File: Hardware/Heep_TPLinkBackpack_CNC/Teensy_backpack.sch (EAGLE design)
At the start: 32 parts, among them J1 FEMALE 2x3, Q1 25MHz, Q2 600mA/40V, U1 ENC28J60-SO

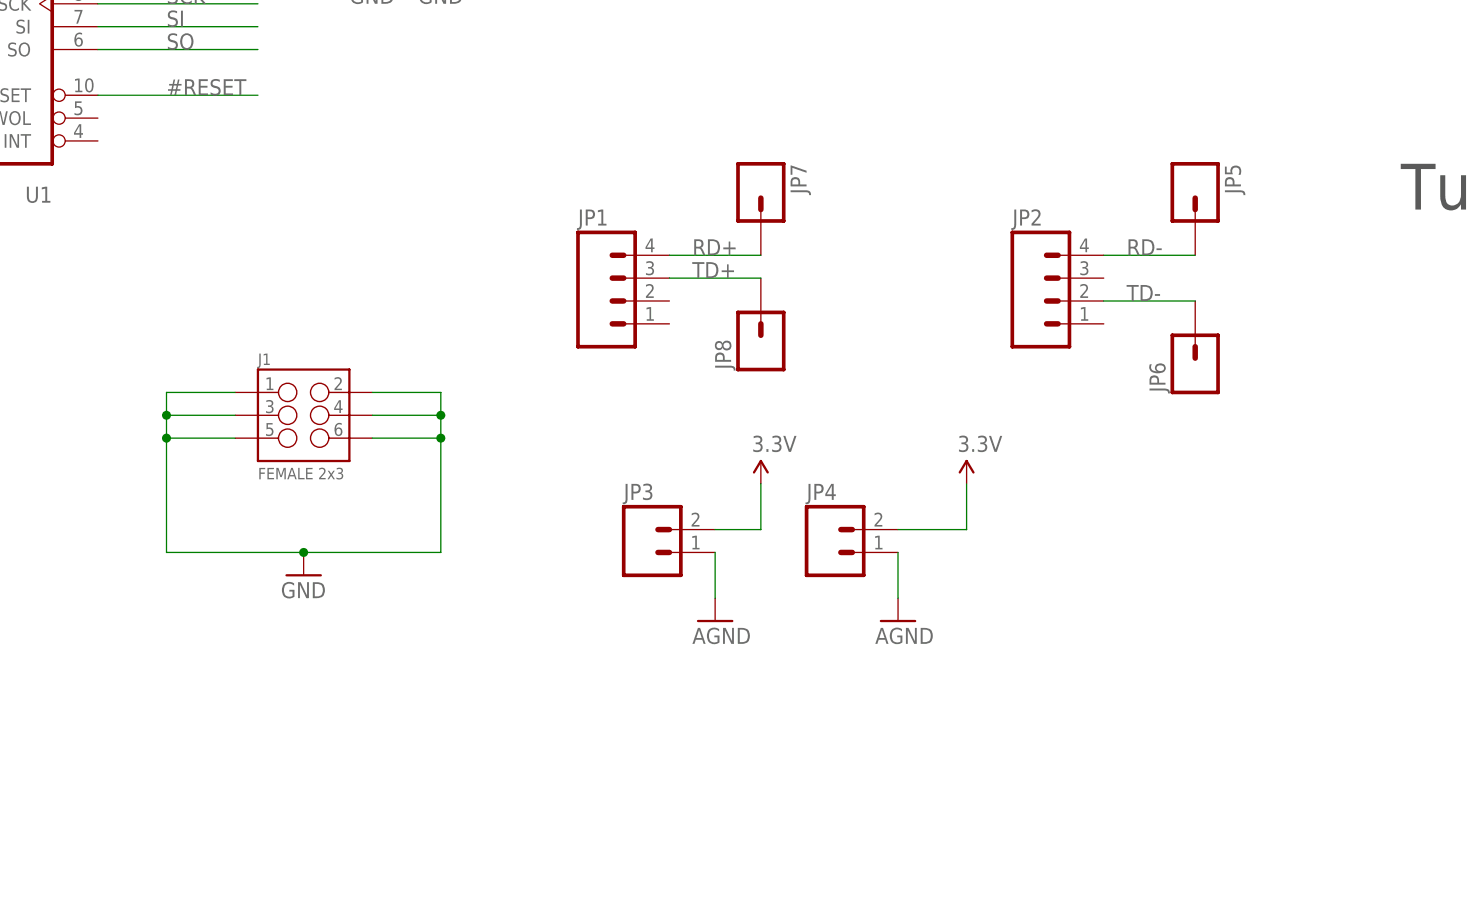
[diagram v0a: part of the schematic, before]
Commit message: #44 changed filename to CNC
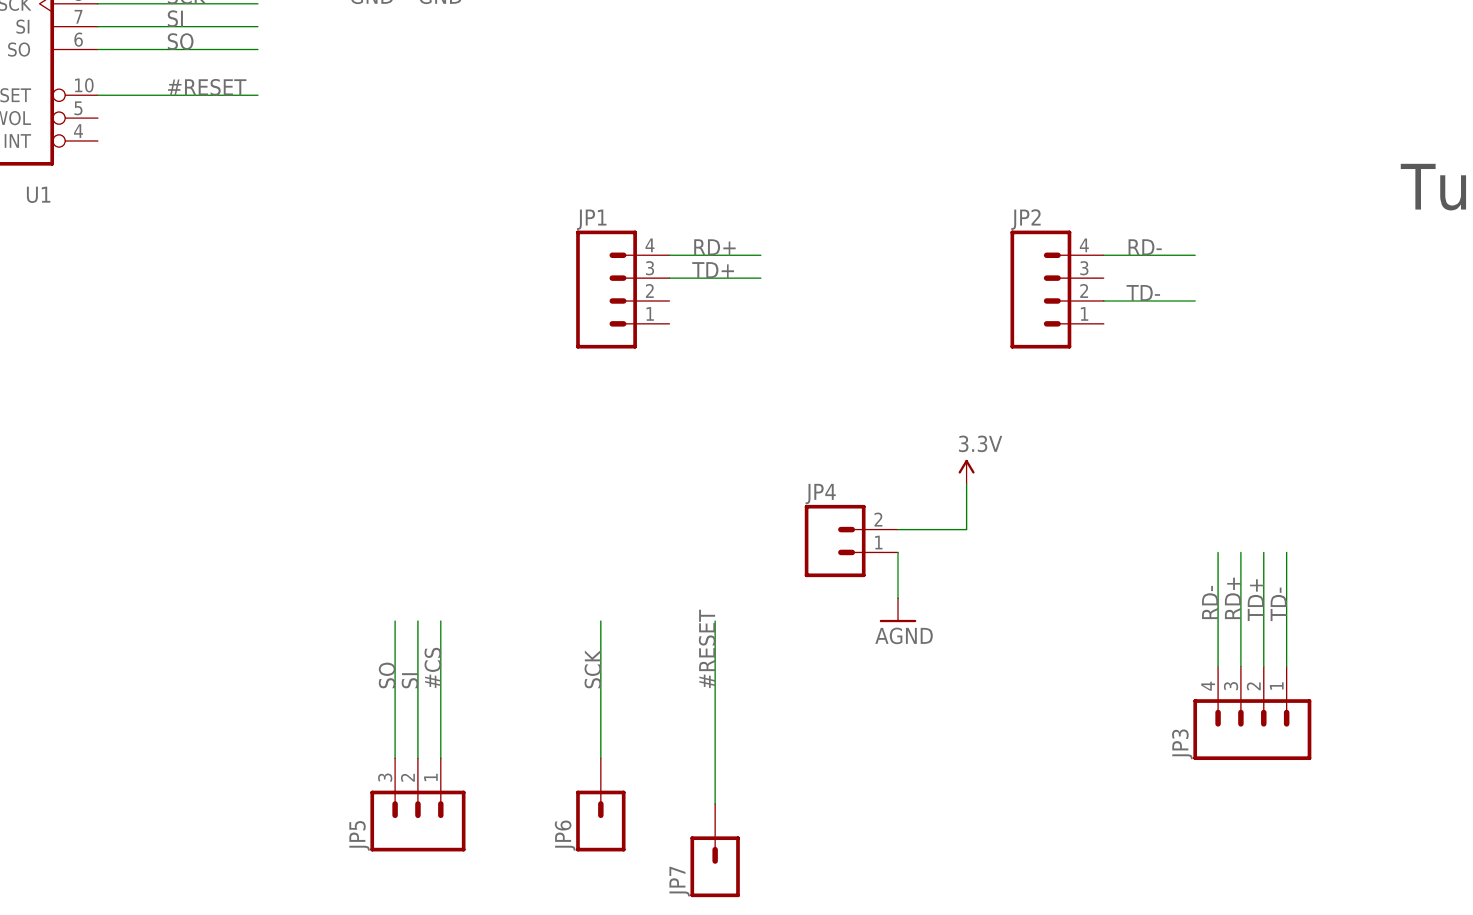
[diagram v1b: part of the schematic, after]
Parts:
- removed J1: FEMALE 2x3, SparkFun-Connectors:M03X2FEMALE
- removed JP8: (no value), SparkFun-Connectors:M01NOSILK-KIT
- JP3: device SparkFun-Connectors:M021X02_NO_SILK -> SparkFun-Connectors:M04NO_SILK_ALL_ROUND
- JP5: device SparkFun-Connectors:M01NOSILK-KIT -> SparkFun-Connectors:M03PTH
- JP6, JP7: device SparkFun-Connectors:M01NOSILK-KIT -> SparkFun-Connectors:M01PTH
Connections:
- net #CS: now also JP5.1
- net #RESET: now also JP7.1
- net 3.3V: no longer JP3.2
- net AGND: no longer JP3.1
- net GND: no longer J1.1, J1.2, J1.3, J1.4, J1.5, J1.6
- net RD+: now also JP3.3; no longer JP7.1
- net RD-: now also JP3.4; no longer JP5.1
- net SCK: now also JP6.1
- net SI: now also JP5.2
- net SO: now also JP5.3
- net TD+: now also JP3.2; no longer JP8.1
- net TD-: now also JP3.1; no longer JP6.1
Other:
- moved on the sheet: JP6, JP7
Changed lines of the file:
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@@
 <part name="JP1" library="SparkFun-Connectors" deviceset="M04" device="NO_SILK_ALL_ROUND"/>
 <part name="JP2" library="SparkFun-Connectors" deviceset="M04" device="NO_SILK_ALL_ROUND"/>
-<part name="JP3" library="SparkFun-Connectors" deviceset="M02" device="1X02_NO_SILK"/>
 <part name="JP4" library="SparkFun-Connectors" deviceset="M02" device="1X02_NO_SILK"/>
-<part name="JP5" library="SparkFun-Connectors" deviceset="M01" device="NOSILK-KIT"/>
-<part name="JP6" library="SparkFun-Connectors" deviceset="M01" device="NOSILK-KIT"/>
-<part name="JP7" library="SparkFun-Connectors" deviceset="M01" device="NOSILK-KIT"/>
-<part name="JP8" library="SparkFun-Connectors" deviceset="M01" device="NOSILK-KIT"/>
 <part name="U1" library="microchip-enc28j60" deviceset="ENC28J60-*" device="SO"/>
 <part name="C1" library="SparkFun-Capacitors" deviceset="CAP" device="0603-CAP" value="0.1uF"/>
@@
 <part name="D1" library="SparkFun-DiscreteSemi" deviceset="DIODE" device="-1N4148" value="200mA/100V/1V"/>
 <part name="D2" library="SparkFun-DiscreteSemi" deviceset="DIODE" device="-1N4148" value="200mA/100V/1V"/>
-<part name="SUPPLY4" library="SparkFun-Aesthetics" deviceset="3.3V" device=""/>
 <part name="SUPPLY5" library="SparkFun-Aesthetics" deviceset="3.3V" device=""/>
 <part name="U$2" library="SparkFun-Aesthetics" deviceset="AGND" device=""/>
-<part name="U$3" library="SparkFun-Aesthetics" deviceset="AGND" device=""/>
 <part name="U$4" library="SparkFun-Aesthetics" deviceset="AGND" device=""/>
 <part name="SUPPLY7" library="SparkFun-Aesthetics" deviceset="3.3V" device=""/>
 <part name="GND1" library="SparkFun-Aesthetics" deviceset="GND" device=""/>
-<part name="J1" library="SparkFun-Connectors" deviceset="M03X2" device="FEMALE" value="FEMALE 2x3"/>
-<part name="GND2" library="SparkFun-Aesthetics" deviceset="GND" device=""/>
 <part name="D3" library="SparkFun-DiscreteSemi" deviceset="DIODE" device="-1N4148" value="200mA/100V/1V"/>
+<part name="JP3" library="SparkFun-Connectors" deviceset="M04" device="NO_SILK_ALL_ROUND"/>
+<part name="JP5" library="SparkFun-Connectors" deviceset="M03" device="PTH"/>
+<part name="JP6" library="SparkFun-Connectors" deviceset="M01" device="PTH"/>
+<part name="JP7" library="SparkFun-Connectors" deviceset="M01" device="PTH"/>
 </parts>
 <sheets>
@@
 <instance part="JP1" gate="G$1" x="43.18" y="63.5"/>
 <instance part="JP2" gate="G$1" x="91.44" y="63.5"/>
-<instance part="JP3" gate="G$1" x="45.72" y="35.56"/>
 <instance part="JP4" gate="G$1" x="66.04" y="35.56"/>
-<instance part="JP5" gate="G$1" x="106.68" y="76.2" rot="R270"/>
-<instance part="JP6" gate="G$1" x="106.68" y="55.88" rot="R90"/>
-<instance part="JP7" gate="G$1" x="58.42" y="76.2" rot="R270"/>
-<instance part="JP8" gate="G$1" x="58.42" y="58.42" rot="R90"/>
 <instance part="U1" gate="G$1" x="-40.64" y="99.06" rot="R180"/>
 <instance part="C1" gate="G$1" x="-99.06" y="50.8"/>
@@
 <instance part="D1" gate="G$1" x="165.1" y="55.88"/>
 <instance part="D2" gate="G$1" x="157.48" y="55.88"/>
-<instance part="SUPPLY4" gate="G$1" x="58.42" y="43.18"/>
 <instance part="SUPPLY5" gate="G$1" x="81.28" y="43.18"/>
 <instance part="U$2" gate="G$1" x="73.66" y="27.94"/>
-<instance part="U$3" gate="G$1" x="53.34" y="27.94"/>
 <instance part="U$4" gate="G$1" x="175.26" y="45.72"/>
 <instance part="SUPPLY7" gate="G$1" x="144.78" y="58.42"/>
 <instance part="GND1" gate="1" x="180.34" y="60.96"/>
-<instance part="J1" gate="G$1" x="7.62" y="50.8"/>
-<instance part="GND2" gate="1" x="7.62" y="33.02"/>
 <instance part="D3" gate="G$1" x="149.86" y="55.88"/>
+<instance part="JP3" gate="G$1" x="114.3" y="17.78" rot="R90"/>
+<instance part="JP5" gate="G$1" x="20.32" y="5.08" rot="R90"/>
+<instance part="JP6" gate="G$1" x="40.64" y="5.08" rot="R90"/>
+<instance part="JP7" gate="G$1" x="53.34" y="0" rot="R90"/>
 </instances>
 <busses>
@@
 <pinref part="GND1" gate="1" pin="GND"/>
 </segment>
-<segment>
-<pinref part="J1" gate="G$1" pin="1"/>
-<wire x1="0" y1="53.34" x2="-7.62" y2="53.34" width="0.1524" layer="91"/>
-<wire x1="-7.62" y1="53.34" x2="-7.62" y2="50.8" width="0.1524" layer="91"/>
-<pinref part="J1" gate="G$1" pin="3"/>
-<wire x1="-7.62" y1="50.8" x2="-7.62" y2="48.26" width="0.1524" layer="91"/>
-<wire x1="0" y1="50.8" x2="-7.62" y2="50.8" width="0.1524" layer="91"/>
-<junction x="-7.62" y="50.8"/>
-<pinref part="J1" gate="G$1" pin="5"/>
-<wire x1="0" y1="48.26" x2="-7.62" y2="48.26" width="0.1524" layer="91"/>
-<junction x="-7.62" y="48.26"/>
-<wire x1="-7.62" y1="48.26" x2="-7.62" y2="35.56" width="0.1524" layer="91"/>
-<pinref part="J1" gate="G$1" pin="2"/>
-<wire x1="15.24" y1="53.34" x2="22.86" y2="53.34" width="0.1524" layer="91"/>
-<wire x1="22.86" y1="53.34" x2="22.86" y2="50.8" width="0.1524" layer="91"/>
-<pinref part="J1" gate="G$1" pin="4"/>
-<wire x1="22.86" y1="50.8" x2="22.86" y2="48.26" width="0.1524" layer="91"/>
-<wire x1="22.86" y1="48.26" x2="22.86" y2="35.56" width="0.1524" layer="91"/>
-<wire x1="15.24" y1="50.8" x2="22.86" y2="50.8" width="0.1524" layer="91"/>
-<junction x="22.86" y="50.8"/>
-<pinref part="J1" gate="G$1" pin="6"/>
-<wire x1="15.24" y1="48.26" x2="22.86" y2="48.26" width="0.1524" layer="91"/>
-<junction x="22.86" y="48.26"/>
-<wire x1="-7.62" y1="35.56" x2="7.62" y2="35.56" width="0.1524" layer="91"/>
-<pinref part="GND2" gate="1" pin="GND"/>
-<wire x1="7.62" y1="35.56" x2="22.86" y2="35.56" width="0.1524" layer="91"/>
-<junction x="7.62" y="35.56"/>
-</segment>
 </net>
 <net name="RD+" class="0">
@@
 <segment>
 <pinref part="JP1" gate="G$1" pin="4"/>
-<pinref part="JP7" gate="G$1" pin="1"/>
 <wire x1="58.42" y1="68.58" x2="48.26" y2="68.58" width="0.1524" layer="91"/>
 <label x="50.8" y="68.58" size="1.778" layer="95"/>
+</segment>
+<segment>
+<pinref part="JP3" gate="G$1" pin="3"/>
+<wire x1="111.76" y1="22.86" x2="111.76" y2="35.56" width="0.1524" layer="91"/>
+<label x="111.76" y="27.94" size="1.778" layer="95" rot="R90"/>
 </segment>
 </net>
@@
 <segment>
 <pinref part="JP2" gate="G$1" pin="4"/>
-<pinref part="JP5" gate="G$1" pin="1"/>
 <wire x1="96.52" y1="68.58" x2="106.68" y2="68.58" width="0.1524" layer="91"/>
 <label x="99.06" y="68.58" size="1.778" layer="95"/>
+</segment>
+<segment>
+<pinref part="JP3" gate="G$1" pin="4"/>
+<wire x1="109.22" y1="22.86" x2="109.22" y2="35.56" width="0.1524" layer="91"/>
+<label x="109.22" y="27.94" size="1.778" layer="95" rot="R90"/>
 </segment>
 </net>
@@
 <segment>
 <pinref part="JP2" gate="G$1" pin="2"/>
-<pinref part="JP6" gate="G$1" pin="1"/>
 <wire x1="106.68" y1="63.5" x2="96.52" y2="63.5" width="0.1524" layer="91"/>
 <label x="99.06" y="63.5" size="1.778" layer="95"/>
+</segment>
+<segment>
+<pinref part="JP3" gate="G$1" pin="1"/>
+<wire x1="116.84" y1="22.86" x2="116.84" y2="35.56" width="0.1524" layer="91"/>
+<label x="116.84" y="27.94" size="1.778" layer="95" rot="R90"/>
 </segment>
 </net>
@@
 <segment>
 <pinref part="JP1" gate="G$1" pin="3"/>
-<pinref part="JP8" gate="G$1" pin="1"/>
 <wire x1="58.42" y1="66.04" x2="48.26" y2="66.04" width="0.1524" layer="91"/>
 <label x="50.8" y="66.04" size="1.778" layer="95"/>
+</segment>
+<segment>
+<pinref part="JP3" gate="G$1" pin="2"/>
+<wire x1="114.3" y1="22.86" x2="114.3" y2="35.56" width="0.1524" layer="91"/>
+<label x="114.3" y="27.94" size="1.778" layer="95" rot="R90"/>
 </segment>
 </net>
@@
 </segment>
 <segment>
-<pinref part="JP3" gate="G$1" pin="2"/>
-<wire x1="53.34" y1="38.1" x2="58.42" y2="38.1" width="0.1524" layer="91"/>
-<wire x1="58.42" y1="38.1" x2="58.42" y2="43.18" width="0.1524" layer="91"/>
-<pinref part="SUPPLY4" gate="G$1" pin="3.3V"/>
-</segment>
-<segment>
 <pinref part="JP4" gate="G$1" pin="2"/>
 <wire x1="73.66" y1="38.1" x2="81.28" y2="38.1" width="0.1524" layer="91"/>
@@
 <wire x1="7.62" y1="144.78" x2="7.62" y2="172.72" width="0.1524" layer="91"/>
 </segment>
+<segment>
+<pinref part="JP5" gate="G$1" pin="1"/>
+<wire x1="22.86" y1="12.7" x2="22.86" y2="27.94" width="0.1524" layer="91"/>
+<label x="22.86" y="20.32" size="1.778" layer="95" rot="R90"/>
+</segment>
 </net>
 <net name="SCK" class="0">
@@
 <label x="30.48" y="137.16" size="1.778" layer="95"/>
 </segment>
+<segment>
+<pinref part="JP6" gate="G$1" pin="1"/>
+<wire x1="40.64" y1="12.7" x2="40.64" y2="27.94" width="0.1524" layer="91"/>
+<label x="40.64" y="20.32" size="1.778" layer="95" rot="R90"/>
+</segment>
 </net>
 <net name="SI" class="0">
@@
 <label x="30.48" y="142.24" size="1.778" layer="95"/>
 </segment>
+<segment>
+<pinref part="JP5" gate="G$1" pin="2"/>
+<wire x1="20.32" y1="12.7" x2="20.32" y2="27.94" width="0.1524" layer="91"/>
+<label x="20.32" y="20.32" size="1.778" layer="95" rot="R90"/>
+</segment>
 </net>
 <net name="SO" class="0">
@@
 <wire x1="48.26" y1="139.7" x2="30.48" y2="139.7" width="0.1524" layer="91"/>
 <label x="30.48" y="139.7" size="1.778" layer="95"/>
+</segment>
+<segment>
+<pinref part="JP5" gate="G$1" pin="3"/>
+<wire x1="17.78" y1="12.7" x2="17.78" y2="27.94" width="0.1524" layer="91"/>
+<label x="17.78" y="20.32" size="1.778" layer="95" rot="R90"/>
 </segment>
 </net>
@@
 <wire x1="22.86" y1="165.1" x2="22.86" y2="172.72" width="0.1524" layer="91"/>
 </segment>
+<segment>
+<wire x1="53.34" y1="7.62" x2="53.34" y2="27.94" width="0.1524" layer="91"/>
+<label x="53.34" y="20.32" size="1.778" layer="95" rot="R90"/>
+<pinref part="JP7" gate="G$1" pin="1"/>
+</segment>
 </net>
 <net name="AGND" class="0">
@@
 </segment>
 <segment>
-<pinref part="JP3" gate="G$1" pin="1"/>
-<wire x1="53.34" y1="30.48" x2="53.34" y2="35.56" width="0.1524" layer="91"/>
-<pinref part="U$3" gate="G$1" pin="AGND"/>
-</segment>
-<segment>
